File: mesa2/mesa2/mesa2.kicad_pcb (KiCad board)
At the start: 2 copper layers, 242 x 111 mm, 53 parts, among them J2 Tag-Connect TC2030

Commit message: Update the mesa2 PCB from the Rev B schematic
Ran Update PCB from Schematic in KiCad: the four outer-pinky footprints
are gone and every right-hand diode's cathode moved to the column its
finger uses on the left. The board now agrees with the schematic on 18
keys and per-finger columns.

Key placement is untouched -- the pinky rotation and the thumb move are
a separate step. The right-side column routing is stale by construction
and gets redone with the rest of the key routing.

Assisted-by: Claude:opus-5
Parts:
- removed D_LR1, D_RR1: 1N4148W, Diode_SMD:D_SOD-123
- removed SW_LR1, SW_RR1: SW_PG1350, mesa1:Kailh_socket_PG1350
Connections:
- D_RA1 pad 1: /COL_4 -> /COL_1
- D_RE1 pad 1: /COL_1 -> /COL_4
- D_RI1 pad 1: /COL_1 -> /COL_4
- D_RN1 pad 1: /COL_2 -> /COL_3
- D_RO1 pad 1: /COL_3 -> /COL_2
- D_RS1 pad 1: /COL_3 -> /COL_2
- D_RT1 pad 1: /COL_2 -> /COL_3
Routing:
- net (no net): track 0.00 -> 23.4 mm
- net Net-(D_LR1-A): track 11.8 -> 0.00 mm
- net Net-(D_RR1-A): track 11.7 -> 0.00 mm

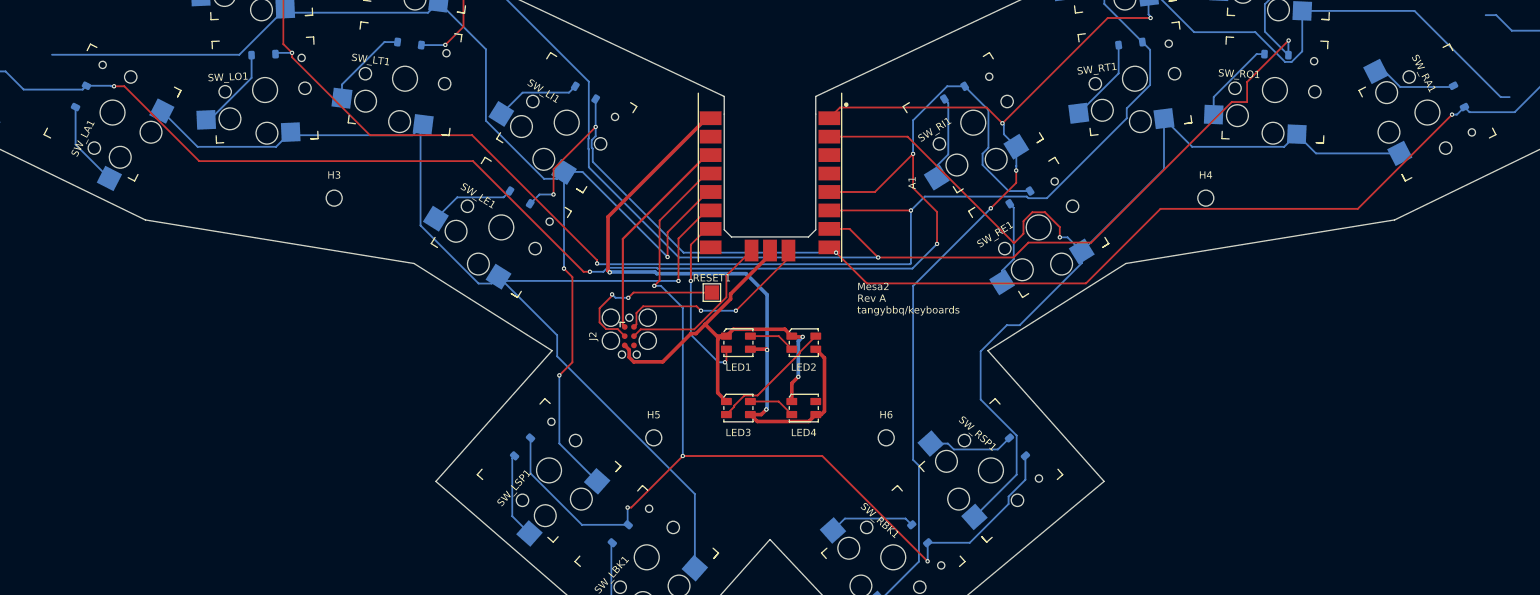
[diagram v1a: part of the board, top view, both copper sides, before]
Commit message: Apply the Rev B key placement
Rotate the surviving pinky keys 90 degrees and pull the SP thumb keys
1 mm in toward BK, with each diode following its switch. Eight
footprints move; the other 28 were already correct.

Konnect's IPC path is the normal route for this, but it segfaults KiCad
10.0.5 here on writes and on read-only queries alike, so apply-revb.py
does it through KiCad's own pcbnew module instead -- the board is loaded
and written by KiCad's serializer, not by touching the file as text. The
diff stays inside the eight footprints and the board's structure is
unchanged: 50 footprints, 401 segments, 41 vias, one zone.

revb.py grows a guard, since it transforms Rev A and is not idempotent.

Assisted-by: Claude:opus-5
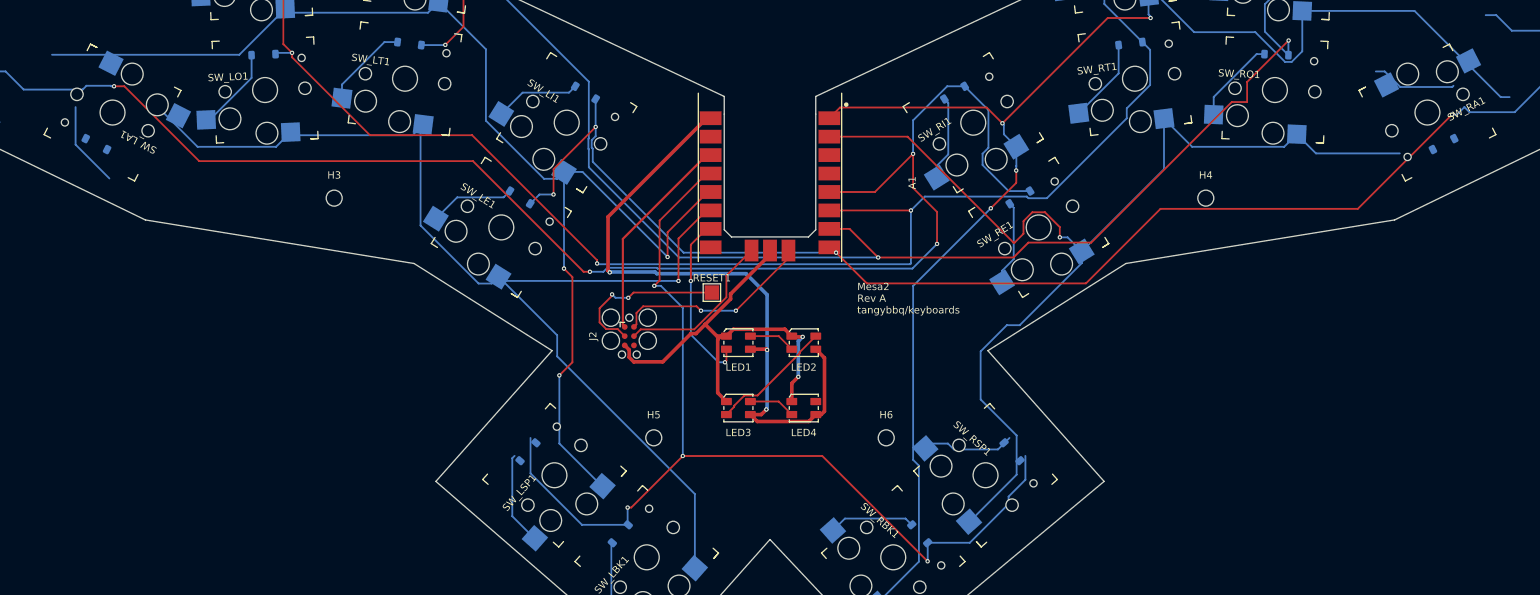
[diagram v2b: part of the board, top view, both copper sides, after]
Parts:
- moved D_LA1 6.90 mm to (42.3, 64.6), turned to -27.1 degrees
- moved D_RA1 6.90 mm to (227.7, 64.6), turned to 27.1 degrees
- moved D_LSP1 1.00 mm to (101.7, 106.9)
- moved D_RSP1 1.00 mm to (168.3, 106.9)
- moved SW_LSP1 1.00 mm to (105.3, 110.2)
- moved SW_RSP1 1.00 mm to (164.7, 110.2)
- turned SW_LA1 to 152.9 degrees
- turned SW_RA1 to -152.9 degrees
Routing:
- net Net-(D_RA1-A): track 11.7 -> 0.00 mm
- net /ROW_D: track 153.3 -> 164.9 mm

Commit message: Rotate the pinky keys the other way
Both pinky keys were turned the wrong way: -90 on the left and +90 on
the right is what the board wants, not the reverse. The keycap lands in
the same place either way, since the two options are 180 degrees apart
and the cap is a rectangle, so every clearance number is identical and
nothing in the geometry could have picked between them. What differs is
which side the socket body and the diode sit on, which is visible on the
board and not in the numbers. LAYOUT.md now says so, to stop the
clearance table arguing for the wrong one later.

revb.py can recover Rev A from git now that the working board has moved
past it, so regenerating the placement no longer depends on the board
being in its pre-Rev-B state.

Assisted-by: Claude:opus-5
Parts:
- moved D_RA1 9.75 mm to (223.3, 55.9), turned to -152.9 degrees
- moved D_LA1 9.75 mm to (46.7, 55.9), turned to 152.9 degrees
- turned SW_LA1 to -27.1 degrees
- turned SW_RA1 to 27.1 degrees
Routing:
- net Net-(D_RA1-A): track 0.00 -> 11.7 mm
- net /ROW_D: track 164.9 -> 153.3 mm

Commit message: Record the Rev B design review
The board passes: DRC has no errors, schematic parity is clean, the
outline closes through the Tiny2040 cutout, all 36 footprints still sit
where revb-placement.json puts them, and the silkscreen carries the rev.

Correct the GPIO map in LAYOUT.md, which still claimed the columns ran
GP4 up to GP7. They run GP7 down to GP4 now, reassigned after the
columns paired by finger, and the firmware reads that table.

Assisted-by: Claude:opus-5
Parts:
- moved H1 7.81 mm to (50.0, 45.0)
- moved H2 7.81 mm to (220.0, 45.0)
- turned J2 to 90 degrees
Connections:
- A1 pad 4: /COL_1 -> /COL_4
- A1 pad 5: /COL_2 -> /COL_3
- A1 pad 6: /COL_3 -> /COL_2
- A1 pad 7: /COL_4 -> /COL_1
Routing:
- net /COL_2: track 205.6 -> 249.2 mm
- net /ROW_A: track 166.9 -> 124.1 mm
- net /COL_1: track 211.6 -> 245.9 mm, vias 4 -> 2
- net /ROW_C: track 195.0 -> 162.1 mm, vias 4 -> 3
- net (no net): track 23.4 -> 0.00 mm
- net /COL_5: track 142.0 -> 165.2 mm, vias 4 -> 1
- net /COL_3: track 211.4 -> 230.0 mm, vias 4 -> 5
- net /+5V: track 91.4 -> 74.0 mm
- net /GND: track 63.5 -> 76.9 mm, vias 2 -> 3
- net /+3V3: track 29.1 -> 41.9 mm, vias 0 -> 2
- net /ROW_D: track 153.3 -> 165.9 mm
- net /ROW_B: track 156.4 -> 166.5 mm, vias 1 -> 2
- net /RUN: track 23.1 -> 14.0 mm, vias 2 -> 0
- net /SWCLK: track 22.8 -> 30.8 mm
- net /SWDIO: track 27.7 -> 32.3 mm, vias 2 -> 0
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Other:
- board size 242 x 111 mm -> 214 x 111 mm
- board text added: "Mesa2 Rev B tangybbq/keyboards"
- board text removed: "Mesa2 Rev A tangybbq/keyboards"

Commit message: Finish mesa2 Rev B
Rev B is complete: 18 keys with the outer pinky gone, the pinky caps
turned to line up with the other fingers, the thumbs on the same 17 mm
pitch as the finger rows, and columns paired by finger so one keymap
serves this board and the Mesa 3 alike.

Design the SK6812 supply fix in, rather than leaving it as the hand
rework Rev A needed. D_RE2 drops the LED rail to ~4.3 V so the RP2040's
3.3 V data clears the 0.7*VDD threshold, JP1 sits open across it as an
escape hatch for a lot that does not need the drop, and C1-C4 decouple
each LED. LAYOUT.md records why, since Mesa 3 inherits this circuit and
the reasoning is not visible in the netlist.

DRC has no errors and schematic parity is clean. ERC gains one benign
entry: +4V5 has no power-output pin driving it, which a PWR_FLAG would
silence.

Assisted-by: Claude:opus-5
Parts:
- added C1: 100nF, Capacitor_SMD:C_0603_1608Metric_Pad1.08x0.95mm_HandSolder, B.Cu at (129.9, 95.9)
- added C2: 100nF, Capacitor_SMD:C_0603_1608Metric_Pad1.08x0.95mm_HandSolder, B.Cu at (129.5, 101.9)
- added C3: 100nF, Capacitor_SMD:C_0603_1608Metric_Pad1.08x0.95mm_HandSolder, B.Cu at (141.3, 92.0)
- added C4: 100nF, Capacitor_SMD:C_0603_1608Metric_Pad1.08x0.95mm_HandSolder, B.Cu at (139.7, 100.0)
- added D_RE2: 1N4148W, Diode_SMD:D_SOD-123, B.Cu at (119.6, 73.5)
- added JP1: SolderJumper_2_Open, Jumper:SolderJumper-2_P1.3mm_Open_RoundedPad1.0x1.5mm, B.Cu at (117.8, 79.0)
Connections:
- LED1 pad 3: /+5V -> /+4V5
- LED2 pad 3: /+5V -> /+4V5
- LED3 pad 3: /+5V -> /+4V5
- LED4 pad 3: /+5V -> /+4V5
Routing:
- net /+4V5: track 0.00 -> 70.1 mm, vias 0 -> 4
- net /+5V: track 74.0 -> 21.5 mm, vias 3 -> 1
- net /GND: track 76.9 -> 86.0 mm, vias 3 -> 5
- net /COL_4: track 186.1 -> 183.1 mm
- net /ROW_B: track 166.5 -> 168.4 mm
- net /COL_1: track 245.9 -> 247.0 mm

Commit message: Tidy the Rev B LED supply and power flags
Rename the LED series diode to D1, out of the matrix-diode naming it
first landed in, where it would have sat beside D_RE1 in the BOM and
read like a key diode. Add PWR_FLAGs to +5V and +4V5, which clears the
"input power pin not driven" reports that inserting a diode in a rail
produces. ERC goes from 12 entries to 10; DRC still has no errors and
parity is clean.

Record in LAYOUT.md what still reports and why, all of it inherited from
Rev A: GND has no flag of its own, A1's GND2 sits on no net, and GND1 has
no copper reaching it. Clearing those three is cosmetic, and worth it
only so that a real problem cannot hide in the noise later.

Assisted-by: Claude:opus-5
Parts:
- renumbered D_RE2 to D1
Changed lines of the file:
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@@
 		(descr "SOD-123")
 		(tags "SOD-123")
-		(property "Reference" "D_RE2"
+		(property "Reference" "D1"
 			(at 0 2 90)
 			(layer "B.SilkS")
